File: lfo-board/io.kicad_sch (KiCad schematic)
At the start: 54 parts

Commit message: wip
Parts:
- removed Q?: 29004, symbol Device:Q_NPN_EBC
- added Q1: MMBT3904, Package_TO_SOT_SMD:SOT-23, symbol Transistor_BJT:MMBT3904
- C1, C10, C11, C2, C3, C4, C5, C6, C7, C8, C9: renamed from C?; footprint (none) -> Capacitor_SMD:C_0603_1608Metric_Pad1.08x0.95mm_HandSolder
- D1: renamed from D?; footprint (none) -> Diode_SMD:D_SMA_Handsoldering
- R1, R10, R11, R12, R13, R14, R15, R16, R17, R18, R19, R2, R20, R21, R22, R23, R24, R25, R26, R27, R28, R29, R3, R4, R5, R6, R7, R8, R9: renamed from R?; footprint (none) -> Resistor_SMD:R_0603_1608Metric_Pad0.98x0.95mm_HandSolder
- SW1: renamed from SW?; footprint (none) -> Button_Switch_SMD:SW_MEC_5GSH9; LCSC (none) -> C318884
- U1, U2, U3: renamed from U?; footprint (none) -> Package_SO:SOIC-8_3.9x4.9mm_P1.27mm
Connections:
- net GND: now also Q1.2 (E)
- net TapOut: now also Q1.3 (C)
- net at D1.1 (K), R5.2: now also Q1.1 (B)

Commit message: Before removing attenuverters
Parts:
- SW1: footprint Button_Switch_SMD:SW_MEC_5GSH9 -> Button_Switch_SMD:SW_Push_SPST_NO_Alps_SKRK; LCSC C318884 -> C455280
- U1: footprint Package_SO:SOIC-8_3.9x4.9mm_P1.27mm -> Package_SO:SOIC-14_3.9x8.7mm_P1.27mm
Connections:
- net +4.5V: now also U2.3 (+), U2.5 (+); no longer U2.3 (+), U2.5 (+)
- net at C4.1, R10.2, R11.2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: now also U2.2 (-); no longer U2.6 (-)
- net at C4.2, R13.2, R15.1: now also U2.1; no longer U2.7
- net at C3.1, R12.1, R6.2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: now also U2.6 (-); no longer U2.2 (-)
- net at C3.2, R12.2, R14.1: now also U2.7; no longer U2.1
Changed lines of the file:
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@@
     (property "Reference" "U1" (id 0) (at 58.42 93.98 0))
     (property "Value" "OPA4991" (id 1) (at 58.42 96.52 0))
-    (property "Footprint" "Package_SO:SOIC-8_3.9x4.9mm_P1.27mm" (id 2) (at 58.42 104.14 0)
+    (property "Footprint" "Package_SO:SOIC-14_3.9x8.7mm_P1.27mm" (id 2) (at 58.42 104.14 0)
       (effects (font (size 1.27 1.27)) hide)
     )
@@
     (property "Reference" "U1" (id 0) (at 58.42 43.18 0))
     (property "Value" "OPA4991" (id 1) (at 58.42 45.72 0))
-    (property "Footprint" "Package_SO:SOIC-8_3.9x4.9mm_P1.27mm" (id 2) (at 58.42 53.34 0)
+    (property "Footprint" "Package_SO:SOIC-14_3.9x8.7mm_P1.27mm" (id 2) (at 58.42 53.34 0)
       (effects (font (size 1.27 1.27)) hide)
     )
@@
       (effects (font (size 1.27 1.27)) (justify left))
     )
-    (property "Footprint" "Package_SO:SOIC-8_3.9x4.9mm_P1.27mm" (id 2) (at 276.86 45.72 0)
+    (property "Footprint" "Package_SO:SOIC-14_3.9x8.7mm_P1.27mm" (id 2) (at 276.86 45.72 0)
       (effects (font (size 1.27 1.27)) hide)
     )
@@
     (pin "4")
   )
-  (symbol (lib_id "Amplifier_Operational:MCP6002-xSN") (at 93.98 106.68 0) (mirror x) (unit 2)
+  (symbol (lib_id "Amplifier_Operational:MCP6002-xSN") (at 93.98 106.68 0) (mirror x) (unit 1)
     (in_bom yes) (on_board yes) (fields_autoplaced)
     (property "Reference" "U2" (id 0) (at 93.98 96.52 0))
@@
     (pin "2")
   )
-  (symbol (lib_id "Amplifier_Operational:MCP6002-xSN") (at 93.98 55.88 0) (mirror x) (unit 1)
+  (symbol (lib_id "Amplifier_Operational:MCP6002-xSN") (at 93.98 55.88 0) (mirror x) (unit 2)
     (in_bom yes) (on_board yes) (fields_autoplaced)
     (property "Reference" "U2" (id 0) (at 93.98 45.72 0))
@@
     (property "Reference" "U1" (id 0) (at 160.02 43.18 0))
     (property "Value" "OPA4991" (id 1) (at 160.02 45.72 0))
-    (property "Footprint" "Package_SO:SOIC-8_3.9x4.9mm_P1.27mm" (id 2) (at 160.02 53.34 0)
+    (property "Footprint" "Package_SO:SOIC-14_3.9x8.7mm_P1.27mm" (id 2) (at 160.02 53.34 0)
       (effects (font (size 1.27 1.27)) hide)
     )
@@
       (effects (font (size 1.27 1.27)) (justify right))
     )
-    (property "Footprint" "Button_Switch_SMD:SW_MEC_5GSH9" (id 2) (at 96.52 157.48 0)
+    (property "Footprint" "Button_Switch_SMD:SW_Push_SPST_NO_Alps_SKRK" (id 2) (at 96.52 157.48 0)
       (effects (font (size 1.27 1.27)) hide)
     )
@@
       (effects (font (size 1.27 1.27)) hide)
     )
-    (property "LCSC" "C318884" (id 4) (at 101.6 157.48 90)
+    (property "LCSC" "C455280" (id 4) (at 101.6 157.48 90)
       (effects (font (size 1.27 1.27)) hide)
     )
@@
     (property "Reference" "U1" (id 0) (at 160.02 93.98 0))
     (property "Value" "OPA4991" (id 1) (at 160.02 96.52 0))
-    (property "Footprint" "Package_SO:SOIC-8_3.9x4.9mm_P1.27mm" (id 2) (at 160.02 104.14 0)
-      (effects (font (size 1.27 1.27)) hide)
-    )
+    (property "Footprint" "Package_SO:SOIC-14_3.9x8.7mm_P1.27mm" (id 2) (at 160.02 104.14 0)
+      (effects (font (size 1.27 1.27)) hide)
+    )

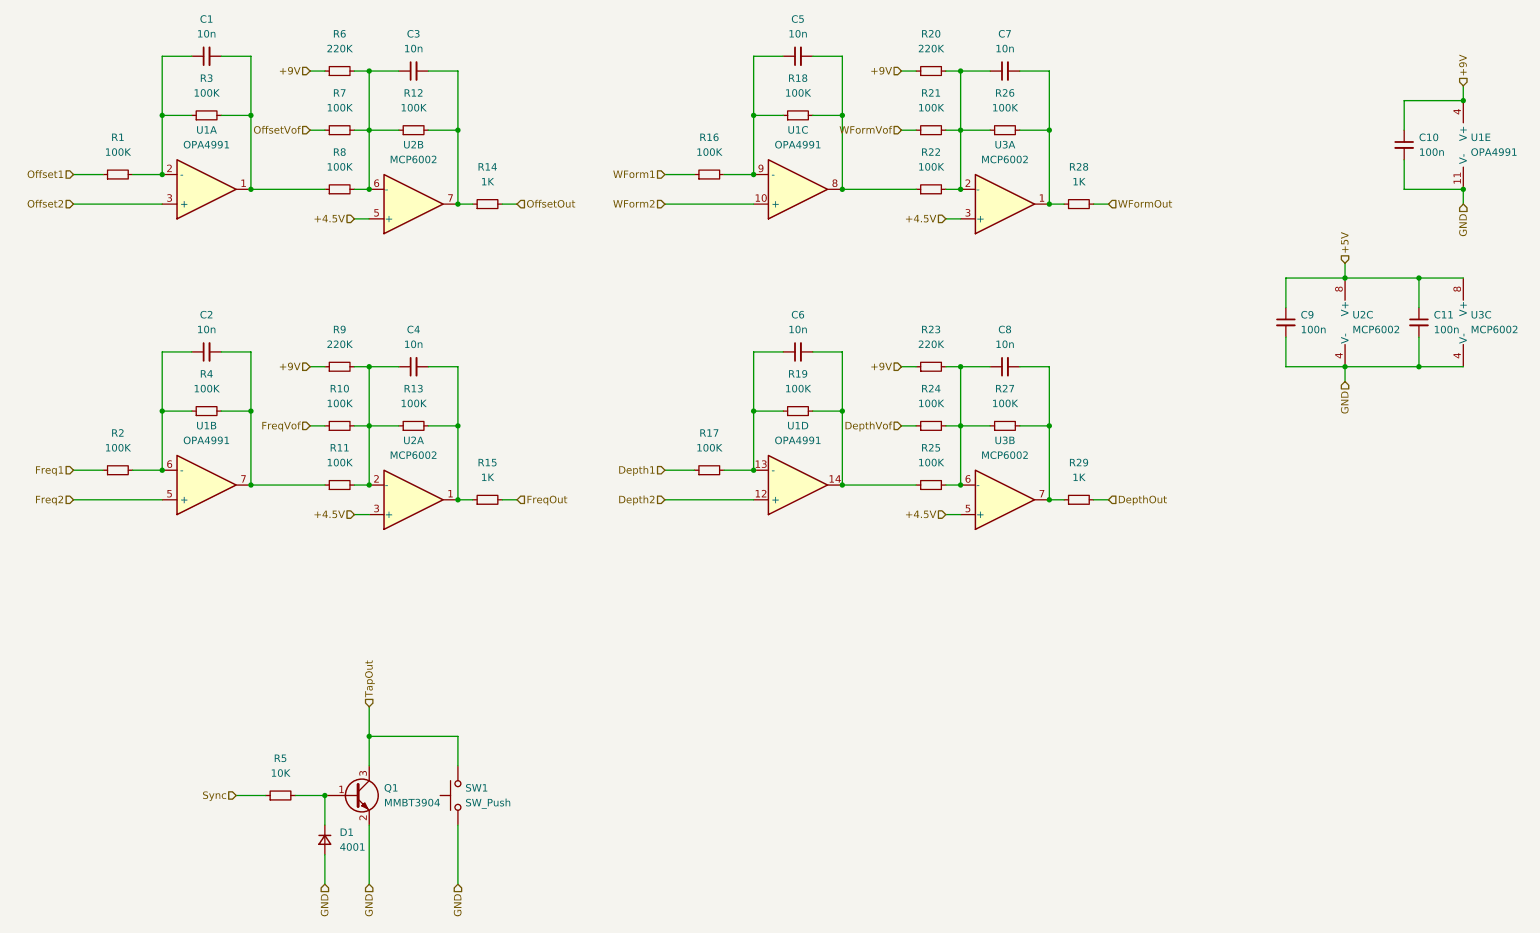
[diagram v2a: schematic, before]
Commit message: LFO graphics
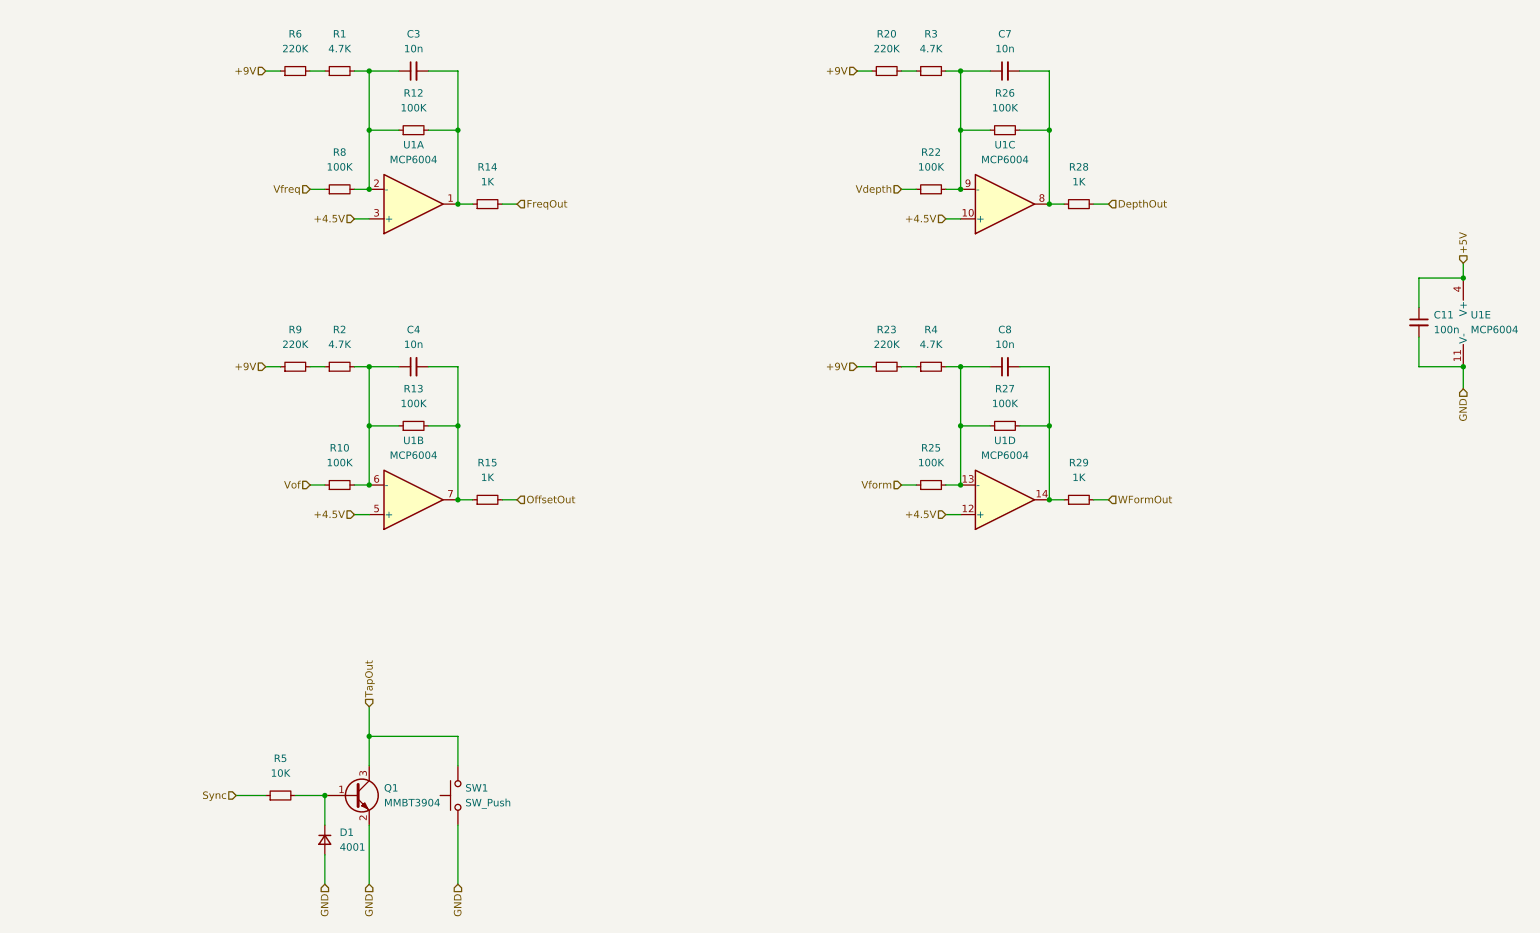
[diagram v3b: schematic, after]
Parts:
- removed C1, C2, C5, C6: 10n, Capacitor_SMD:C_0603_1608Metric_Pad1.08x0.95mm_HandSolder, symbol Device:C_Small
- removed C10, C9: 100n, Capacitor_SMD:C_0603_1608Metric_Pad1.08x0.95mm_HandSolder, symbol Device:C_Small
- removed R11, R16, R17, R18, R19, R21, R24, R7: 100K, Resistor_SMD:R_0603_1608Metric_Pad0.98x0.95mm_HandSolder, symbol Device:R_Small
- removed U1: OPA4991, Package_SO:SOIC-14_3.9x8.7mm_P1.27mm, symbol Device:Opamp_Quad
- removed U2, U3: MCP6002, Package_SO:SOIC-8_3.9x4.9mm_P1.27mm, symbol Amplifier_Operational:MCP6002-xSN
- added U1: MCP6004, symbol Amplifier_Operational:MCP6004
- R1, R2, R3, R4: value 100K -> 4.7K
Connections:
- net +4.5V: now also U1.10 (+), U1.12 (+), U1.3 (+), U1.5 (+)
- net +5V: now also U1.4 (V+)
- net DepthOut: now also R28.2; no longer R29.2
- net FreqOut: now also R14.2; no longer R15.2
- net GND: now also U1.11 (V-)
- net OffsetOut: now also R15.2; no longer R14.2
- net WFormOut: now also R29.2; no longer R28.2
- net at C8.1, R25.2, R27.1: now also R4.2, U1.13 (-); no longer R23.2
- net at C8.2, R27.2, R29.1: now also U1.14
- net Vform: now reaches R25.1
- net at C4.1, R10.2, R13.1: now also R2.2, U1.6 (-); no longer R9.2
- net at C4.2, R13.2, R15.1: now also U1.7
- net Vdepth: now reaches R22.1
- net at C7.2, R26.2, R28.1: now also U1.8
- net at C7.1, R22.2, R26.1: now also R3.2, U1.9 (-); no longer R20.2
- net at R4.1: now also R23.2; no longer R2.2
- net Vfreq: now reaches R8.1
- net Vfreq: no longer R3.2
- net at R1.2: now also C3.1, R12.1, R8.2, U1.2 (-); no longer R3.1
- net at C3.2, R12.2, R14.1: now also U1.1
- net Freq1: no longer names the net of R2.1
- net Freq1: now also R9.2
- net FreqVof renamed Vof
- net Offset1: no longer names the net of R1.1
- net Offset1: now also R6.2
- new net: R20.2, R3.1
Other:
- moved on the sheet: R10, R20, R23, R6, R9

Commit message: LFO board jlc
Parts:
- C11: LCSC (none) -> C497032
- C3, C4, C7, C8: LCSC (none) -> C57112
- D1: LCSC (none) -> C122841
- Q1: LCSC (none) -> C20526
- R1, R2, R3, R4: LCSC (none) -> C23162
- R10, R12, R13, R22, R25, R26, R27, R8: LCSC (none) -> C25803
- R14, R15, R28, R29: LCSC (none) -> C21190
- R20, R23, R6, R9: LCSC (none) -> C22961
- R5: LCSC (none) -> C25804
- U1: footprint (none) -> Package_SO:SOIC-14_3.9x8.7mm_P1.27mm; LCSC (none) -> C7378
- U1: LCSC (none) -> C7378
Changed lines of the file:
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@@
+      (effects (font (size 1.27 1.27)) hide)
+    )
+    (property "LCSC" "C21190" (id 4) (at 208.28 106.68 0)
       (effects (font (size 1.27 1.27)) hide)
     )
@@
       (effects (font (size 1.27 1.27)) hide)
     )
+    (property "LCSC" "C25803" (id 4) (at 182.88 104.14 0)
+      (effects (font (size 1.27 1.27)) hide)
+    )
     (pin "1")
     (pin "2")
@@
       (effects (font (size 1.27 1.27)) hide)
     )
+    (property "LCSC" "C25803" (id 4) (at 93.98 93.98 0)
+      (effects (font (size 1.27 1.27)) hide)
+    )
     (pin "1")
     (pin "2")
@@
       (effects (font (size 1.27 1.27)) hide)
     )
+    (property "LCSC" "C23162" (id 4) (at 81.28 33.02 0)
+      (effects (font (size 1.27 1.27)) hide)
+    )
     (pin "1")
     (pin "2")
@@
       (effects (font (size 1.27 1.27)) hide)
     )
+    (property "LCSC" "C21190" (id 4) (at 106.68 106.68 0)
+      (effects (font (size 1.27 1.27)) hide)
+    )
     (pin "1")
     (pin "2")
@@
       (effects (font (size 1.27 1.27)) hide)
     )
+    (property "LCSC" "C23162" (id 4) (at 182.88 83.82 0)
+      (effects (font (size 1.27 1.27)) hide)
+    )
     (pin "1")
     (pin "2")
@@
       (effects (font (size 1.27 1.27)) hide)
     )
+    (property "LCSC" "C25803" (id 4) (at 195.58 43.18 0)
+      (effects (font (size 1.27 1.27)) hide)
+    )
     (pin "1")
     (pin "2")
@@
       (effects (font (size 1.27 1.27)) hide)
     )
+    (property "LCSC" "C25803" (id 4) (at 195.58 93.98 0)
+      (effects (font (size 1.27 1.27)) hide)
+    )
     (pin "1")
     (pin "2")
@@
     )
     (property "Datasheet" "~" (id 3) (at 78.74 165.1 90)
+      (effects (font (size 1.27 1.27)) hide)
+    )
+    (property "LCSC" "C122841" (id 4) (at 78.74 165.1 0)
       (effects (font (size 1.27 1.27)) hide)
     )
@@
     (property "Reference" "U1" (id 0) (at 93.98 96.52 0))
     (property "Value" "MCP6004" (id 1) (at 93.98 99.06 0))
-    (property "Footprint" "" (id 2) (at 92.71 109.22 0)
+    (property "Footprint" "Package_SO:SOIC-14_3.9x8.7mm_P1.27mm" (id 2) (at 92.71 109.22 0)
       (effects (font (size 1.27 1.27)) hide)
     )
     (property "Datasheet" "http://ww1.microchip.com/downloads/en/DeviceDoc/21733j.pdf" (id 3) (at 95.25 111.76 0)
+      (effects (font (size 1.27 1.27)) hide)
+    )
+    (property "LCSC" "C7378" (id 4) (at 93.98 106.68 0)
       (effects (font (size 1.27 1.27)) hide)
     )
@@
       (effects (font (size 1.27 1.27)) hide)
     )
+    (property "LCSC" "C22961" (id 4) (at 175.26 83.82 0)
+      (effects (font (size 1.27 1.27)) hide)
+    )
     (pin "1")
     (pin "2")
@@
       (effects (font (size 1.27 1.27)) hide)
     )
+    (property "LCSC" "C57112" (id 4) (at 93.98 33.02 0)
+      (effects (font (size 1.27 1.27)) hide)
+    )
     (pin "1")
     (pin "2")
@@
       (effects (font (size 1.27 1.27)) hide)
     )
+    (property "LCSC" "C21190" (id 4) (at 208.28 55.88 0)
+      (effects (font (size 1.27 1.27)) hide)
+    )
     (pin "1")
     (pin "2")
@@
       (effects (font (size 1.27 1.27)) hide)
     )
+    (property "LCSC" "C25803" (id 4) (at 81.28 53.34 0)
+      (effects (font (size 1.27 1.27)) hide)
+    )
     (pin "1")
     (pin "2")
@@
       (effects (font (size 1.27 1.27)) hide)
     )
+    (property "LCSC" "C25803" (id 4) (at 93.98 43.18 0)
+      (effects (font (size 1.27 1.27)) hide)
+    )
     (pin "1")
     (pin "2")
@@
       (effects (font (size 1.27 1.27)) hide)
     )
+    (property "LCSC" "C25804" (id 4) (at 71.12 157.48 0)
+      (effects (font (size 1.27 1.27)) hide)
+    )
     (pin "1")
     (pin "2")
@@
     (property "Reference" "U1" (id 0) (at 195.58 96.52 0))
     (property "Value" "MCP6004" (id 1) (at 195.58 99.06 0))
-    (property "Footprint" "" (id 2) (at 194.31 109.22 0)
+    (property "Footprint" "Package_SO:SOIC-14_3.9x8.7mm_P1.27mm" (id 2) (at 194.31 109.22 0)
       (effects (font (size 1.27 1.27)) hide)
     )
     (property "Datasheet" "http://ww1.microchip.com/downloads/en/DeviceDoc/21733j.pdf" (id 3) (at 196.85 111.76 0)
+      (effects (font (size 1.27 1.27)) hide)
+    )
+    (property "LCSC" "C7378" (id 4) (at 195.58 106.68 0)
       (effects (font (size 1.27 1.27)) hide)
     )
@@
       (effects (font (size 1.27 1.27)) hide)
     )
+    (property "LCSC" "C22961" (id 4) (at 73.66 83.82 0)
+      (effects (font (size 1.27 1.27)) hide)
+    )
     (pin "1")
     (pin "2")
@@
       (effects (font (size 1.27 1.27)) hide)
     )
+    (property "LCSC" "C23162" (id 4) (at 81.28 83.82 0)
+      (effects (font (size 1.27 1.27)) hide)
+    )
     (pin "1")
     (pin "2")
@@
     (property "Reference" "U1" (id 0) (at 93.98 45.72 0))
     (property "Value" "MCP6004" (id 1) (at 93.98 48.26 0))
-    (property "Footprint" "" (id 2) (at 92.71 58.42 0)
+    (property "Footprint" "Package_SO:SOIC-14_3.9x8.7mm_P1.27mm" (id 2) (at 92.71 58.42 0)
       (effects (font (size 1.27 1.27)) hide)
     )
     (property "Datasheet" "http://ww1.microchip.com/downloads/en/DeviceDoc/21733j.pdf" (id 3) (at 95.25 60.96 0)
+      (effects (font (size 1.27 1.27)) hide)
+    )
+    (property "LCSC" "C7378" (id 4) (at 93.98 55.88 0)
       (effects (font (size 1.27 1.27)) hide)
     )
@@
       (effects (font (size 1.27 1.27)) hide)
     )
+    (property "LCSC" "C25803" (id 4) (at 182.88 53.34 0)
+      (effects (font (size 1.27 1.27)) hide)
+    )
     (pin "1")
     (pin "2")
@@
       (effects (font (size 1.27 1.27)) hide)
     )
+    (property "LCSC" "C57112" (id 4) (at 195.58 83.82 0)
+      (effects (font (size 1.27 1.27)) hide)
+    )
     (pin "1")
     (pin "2")
@@
     )
     (property "Datasheet" "~" (id 3) (at 266.7 76.2 0)
+      (effects (font (size 1.27 1.27)) hide)
+    )
+    (property "LCSC" "C497032" (id 4) (at 266.7 76.2 0)
       (effects (font (size 1.27 1.27)) hide)
     )
@@
       (effects (font (size 1.27 1.27)) hide)
     )
+    (property "LCSC" "C22961" (id 4) (at 73.66 33.02 0)
+      (effects (font (size 1.27 1.27)) hide)
+    )
     (pin "1")
     (pin "2")
@@
       (effects (font (size 1.27 1.27)) (justify left))
     )
-    (property "Footprint" "" (id 2) (at 275.59 73.66 0)
+    (property "Footprint" "Package_SO:SOIC-14_3.9x8.7mm_P1.27mm" (id 2) (at 275.59 73.66 0)
       (effects (font (size 1.27 1.27)) hide)
     )
     (property "Datasheet" "http://ww1.microchip.com/downloads/en/DeviceDoc/21733j.pdf" (id 3) (at 278.13 71.12 0)
+      (effects (font (size 1.27 1.27)) hide)
+    )
+    (property "LCSC" "C7378" (id 4) (at 276.86 76.2 0)
       (effects (font (size 1.27 1.27)) hide)
     )
@@
       (effects (font (size 1.27 1.27)) (justify left) hide)
     )
+    (property "LCSC" "C20526" (id 4) (at 83.82 157.48 0)
+      (effects (font (size 1.27 1.27)) hide)
+    )
     (pin "1")
     (pin "2")
@@
       (effects (font (size 1.27 1.27)) hide)
     )
+    (property "LCSC" "C23162" (id 4) (at 182.88 33.02 0)
+      (effects (font (size 1.27 1.27)) hide)
+    )
     (pin "1")
     (pin "2")
@@
       (effects (font (size 1.27 1.27)) hide)
     )
+    (property "LCSC" "C22961" (id 4) (at 175.26 33.02 0)
+      (effects (font (size 1.27 1.27)) hide)
+    )
     (pin "1")
     (pin "2")
@@
       (effects (font (size 1.27 1.27)) hide)
     )
+    (property "LCSC" "C57112" (id 4) (at 93.98 83.82 0)
+      (effects (font (size 1.27 1.27)) hide)
+    )
     (pin "1")
     (pin "2")
@@
     )
     (property "Datasheet" "http://ww1.microchip.com/downloads/en/DeviceDoc/21733j.pdf" (id 3) (at 196.85 60.96 0)
+      (effects (font (size 1.27 1.27)) hide)
+    )
+    (property "LCSC" "C7378" (id 4) (at 195.58 55.88 0)
       (effects (font (size 1.27 1.27)) hide)
     )
@@
       (effects (font (size 1.27 1.27)) hide)
     )
+    (property "LCSC" "C57112" (id 4) (at 195.58 33.02 0)
+      (effects (font (size 1.27 1.27)) hide)
+    )
     (pin "1")
     (pin "2")
@@
       (effects (font (size 1.27 1.27)) hide)
     )
+    (property "LCSC" "C21190" (id 4) (at 106.68 55.88 0)
+      (effects (font (size 1.27 1.27)) hide)
+    )
     (pin "1")
     (pin "2")
@@
       (effects (font (size 1.27 1.27)) hide)
     )
+    (property "LCSC" "C25803" (id 4) (at 81.28 104.14 0)
+      (effects (font (size 1.27 1.27)) hide)
+    )

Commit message: wip pre-redo orientation
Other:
- company: (none) -> Andrey Salomatin / Pedal Markt
- title: (none) -> Longwave
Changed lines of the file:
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@@
 (kicad_sch (version 20211123) (generator eeschema)
   (paper "A4")
+  (title_block
+    (title "Longwave")
+    (date "2024-12-18")
+    (rev "v1rev2")
+    (company "Andrey Salomatin / Pedal Markt")
+  )
   (junction (at 101.6 93.98) (diameter 0) (color 0 0 0 0)
   )
